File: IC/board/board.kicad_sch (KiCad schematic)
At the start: 30 parts, among them SW1 SW_Push, SW2 SW_Push, SW3 SW_Push, SW4 SW_Push, SW5 SW_Push, SW6 Rotary_Encoder_Switch, U2 ATmega328P-PU, Y1 16Mhz

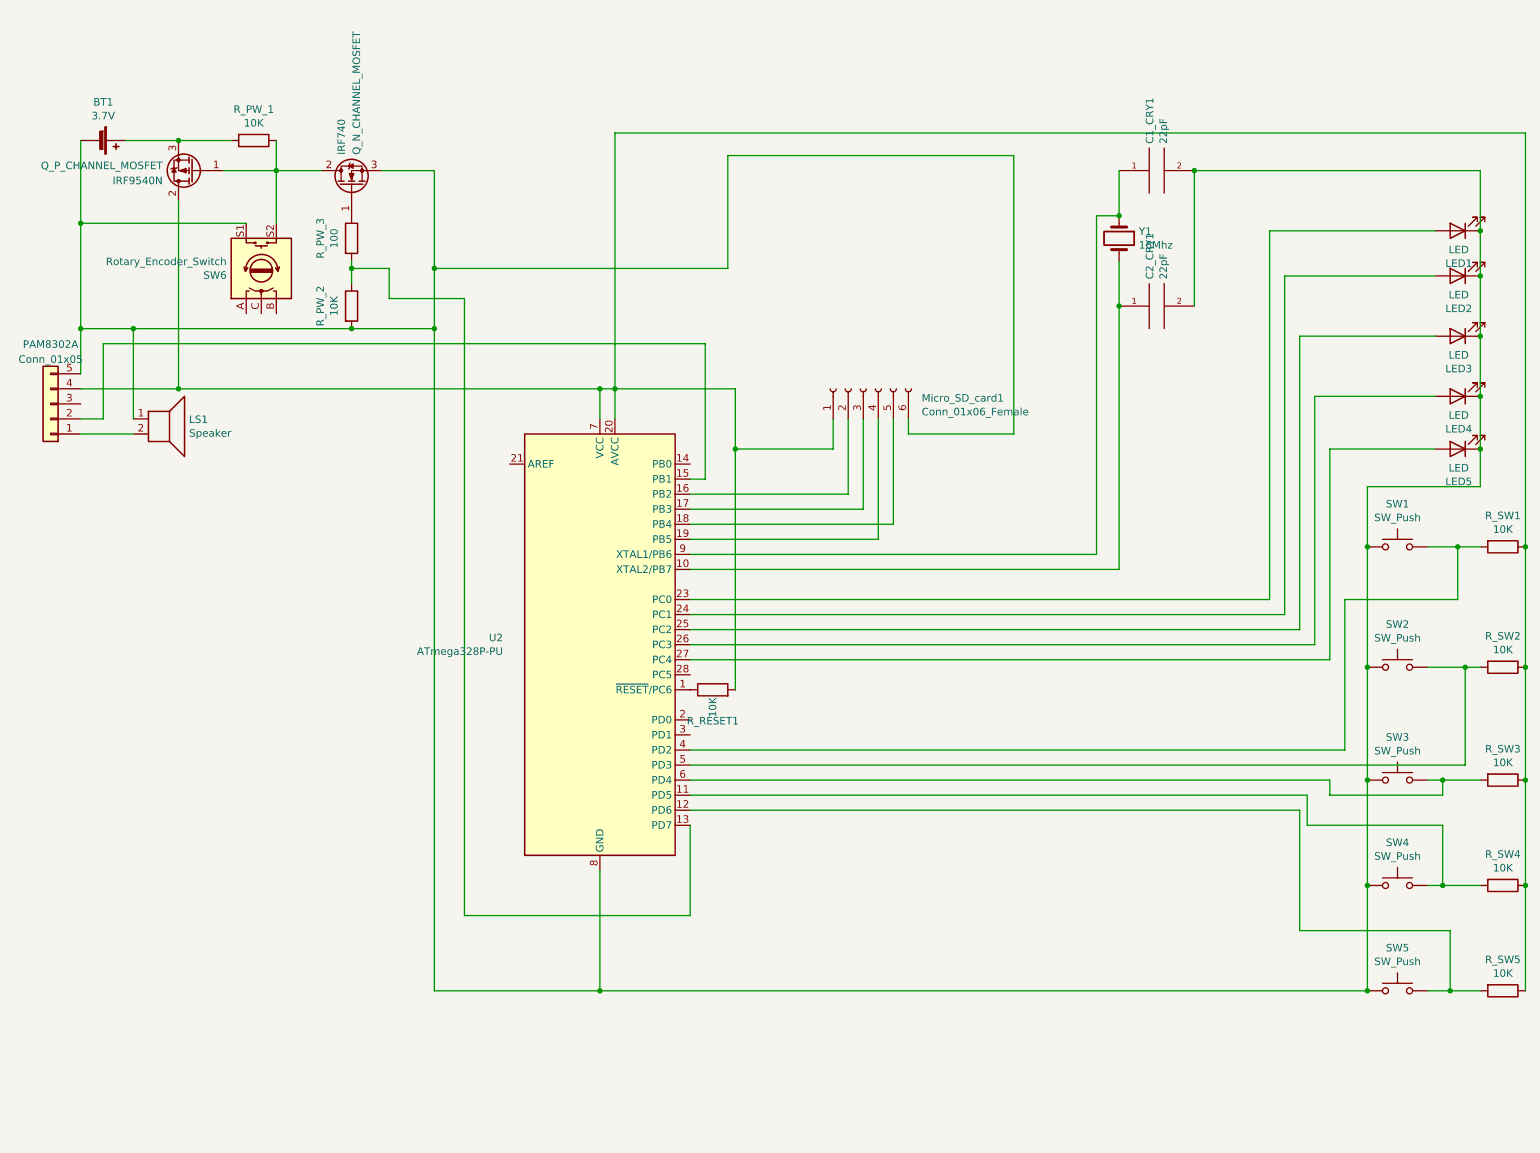
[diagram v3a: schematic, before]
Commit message: Use rotary encoder
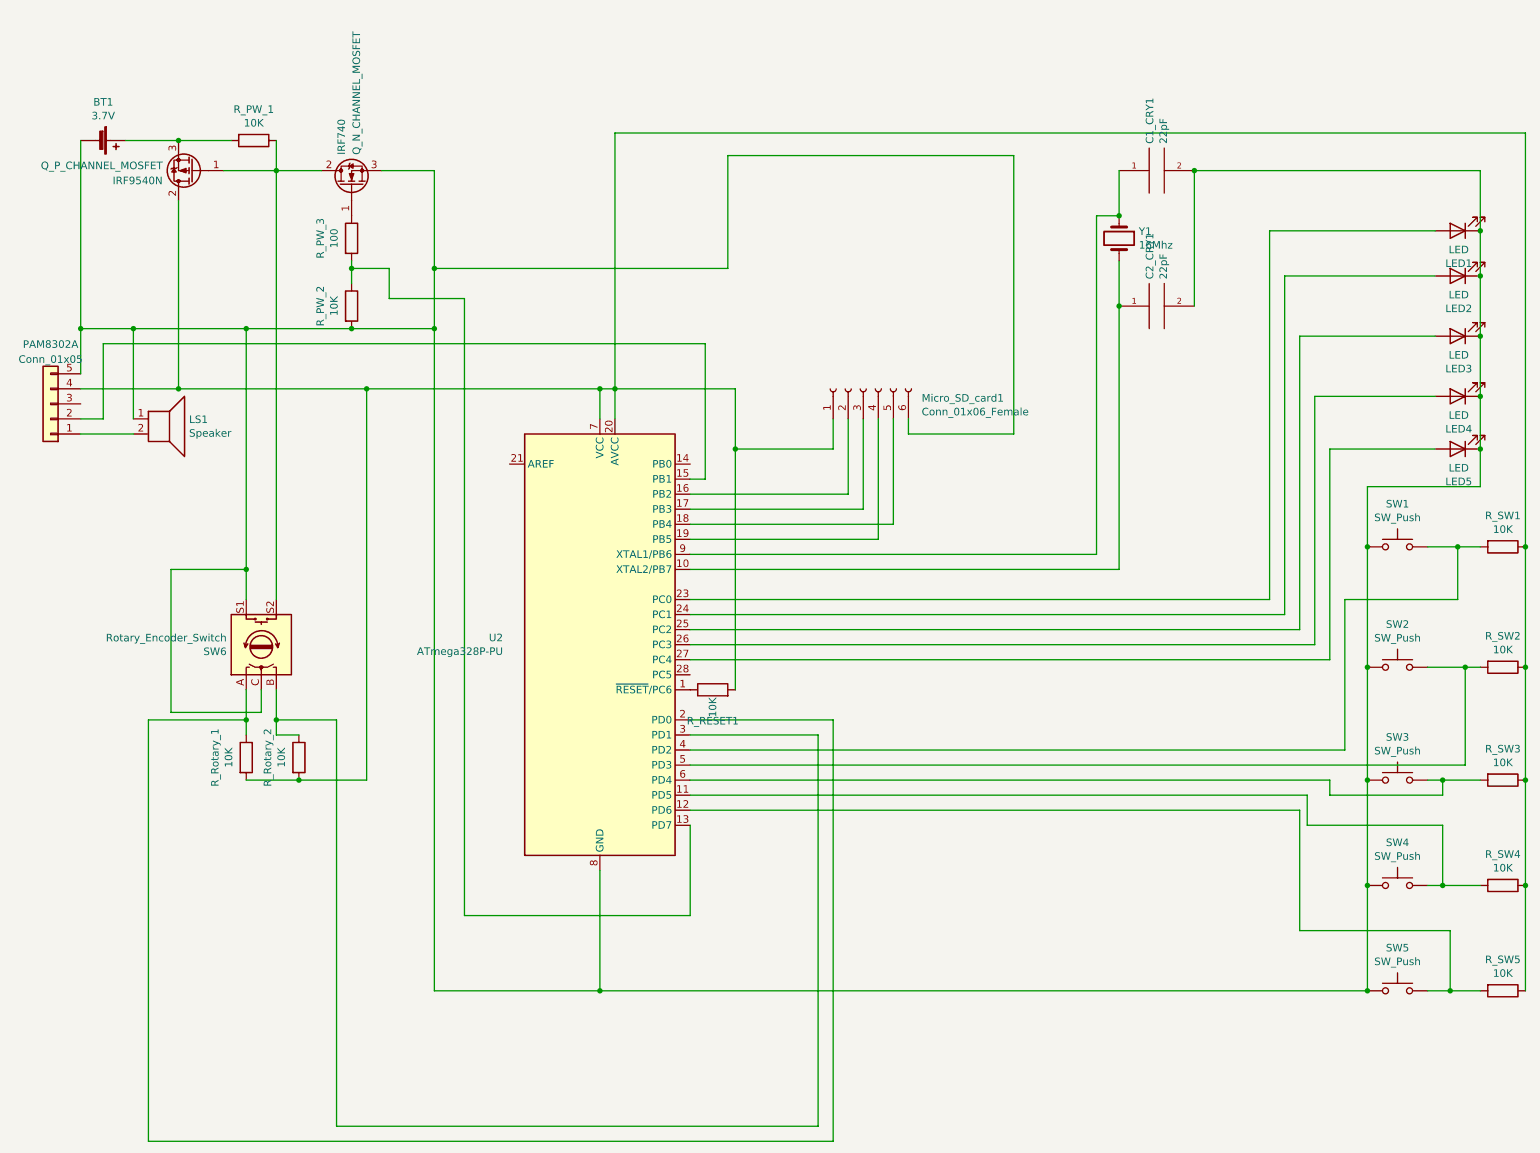
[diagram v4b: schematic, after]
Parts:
- added R_Rotary_1, R_Rotary_2: 10K, Resistor_THT:R_Axial_DIN0207_L6.3mm_D2.5mm_P7.62mm_Horizontal, symbol Device:R
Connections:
- net at Micro_SD_card1.1 (Pin_1), PAM8302A.4 (Pin_4), Q_P_CHANNEL_MOSFET.2 (D)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: now also R_Rotary_1.2, R_Rotary_2.2
- net at BT1.2 (-), C1_CRY1.2, C2_CRY1.2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: now also SW6.C
- net at SW6.A: now also U2.2 (PD0), R_Rotary_1.1
- net at SW6.B: now also U2.3 (PD1), R_Rotary_2.1
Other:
- moved on the sheet: SW6

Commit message: Add diode to control button
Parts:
- added D_1, D_2: DIODE, symbol pspice:DIODE
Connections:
- net at R_PW_2.1, R_PW_3.2: now also D_1.1 (K); no longer U2.13 (PD7)
- net at U2.28 (PC5): now also D_2.1 (K)
- new net: D_1.2 (A), D_2.2 (A), U2.13 (PD7)
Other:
- moved on the sheet: Q_N_CHANNEL_MOSFET, R_PW_2, R_PW_3
